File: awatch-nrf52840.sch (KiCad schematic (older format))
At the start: 26 parts, among them U1 nRF52840, X1 ABM11W-32.0000MHZ-8-B1U-T3

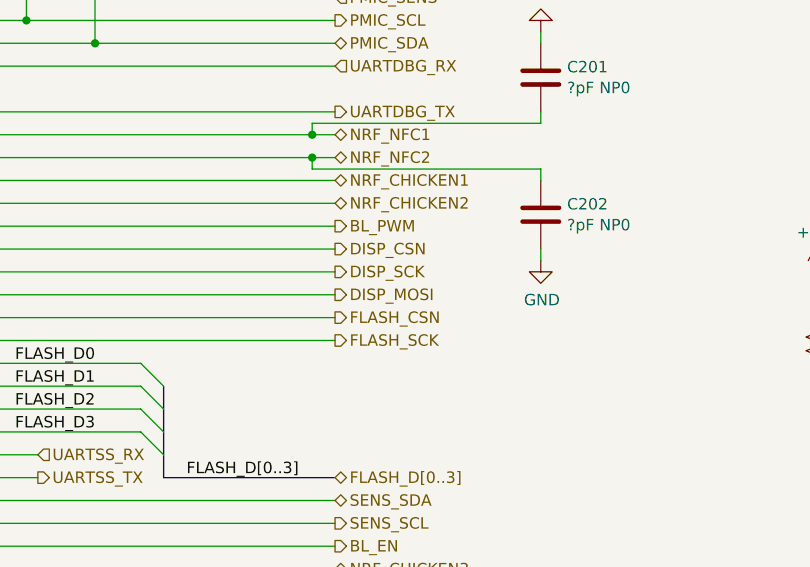
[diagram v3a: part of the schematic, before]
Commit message: fully routed
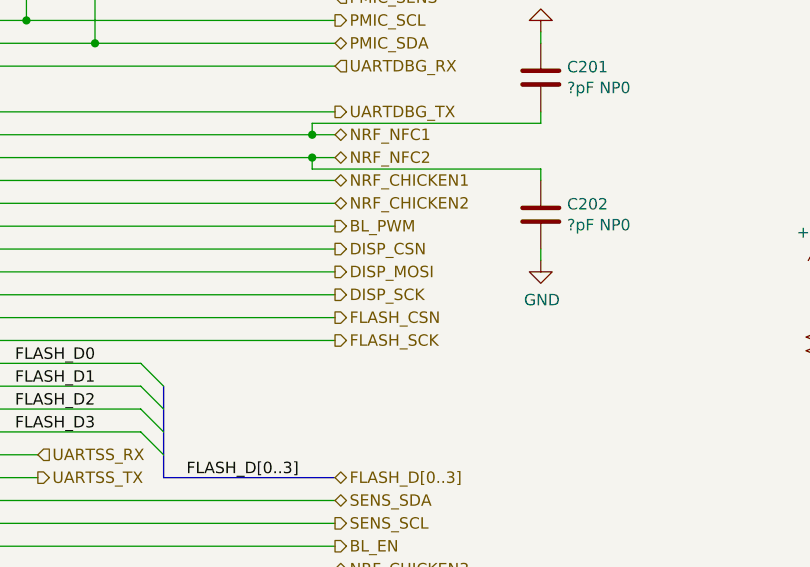
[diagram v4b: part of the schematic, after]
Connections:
- net DISP_MOSI: now also U1.AD10 (P0.15); no longer U1.AC11 (P0.16)
- net DISP_SCK: now also U1.AC11 (P0.16); no longer U1.AD10 (P0.15)
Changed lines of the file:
@@
 Wire Wire Line
 	5150 2500 5650 2500
+Text HLabel 6700 3500 2    50   Output ~ 0
+DISP_MOSI
 Text HLabel 6700 3600 2    50   Output ~ 0
-DISP_MOSI
-Text HLabel 6700 3500 2    50   Output ~ 0
 DISP_SCK
 Text HLabel 6700 3400 2    50   Output ~ 0

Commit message: approx. final layout
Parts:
- C1, C2: DigiKey PN (none) -> 311-3869-1-ND
- C11: DigiKey PN (none) -> 311-1069-1-ND
- C12, C5, C7, C8: value 100nF X7R -> 0.1µF X7R; DigiKey PN (none) -> 1276-1061-1-ND
- C14, C15: DigiKey PN (none) -> 1276-1946-1-ND
- C3, C4: DigiKey PN (none) -> 1276-1293-1-ND
- C6: DigiKey PN (none) -> 1276-2087-1-ND
- C9: DigiKey PN (none) -> 311-3959-1-ND
- U1: DigiKey PN (none) -> 1490-1071-1-ND
- X1: DigiKey PN (none) -> 535-13899-1-ND
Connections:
- net DISP_CSN: now also U1.AC11 (P0.16); no longer U1.AC9 (P0.14)
- net DISP_SCK: now also U1.AC9 (P0.14); no longer U1.AC11 (P0.16)
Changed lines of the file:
@@
 $Descr A4 11693 8268
 encoding utf-8
-Sheet 2 9
+Sheet 2 10
 Title "AWatch2"
 Date ""
@@
 F 2 "Package_DFN_QFN:Nordic_AQFN-73-1EP_7x7mm_P0.5mm" H 3850 1600 50  0001 C CNN
 F 3 "http://infocenter.nordicsemi.com/topic/com.nordic.infocenter.nrf52/dita/nrf52/chips/nrf52840.html" H 3200 6400 50  0001 C CNN
+F 4 "1490-1071-1-ND" H 3850 4500 50  0001 C CNN "DigiKey PN"
 	1    3850 4500
 	1    0    0    -1
@@
 F 2 "Crystal:Crystal_SMD_2016-4Pin_2.0x1.6mm" H 2100 4500 50  0001 C CNN
 F 3 "~" H 2100 4500 50  0001 C CNN
+F 4 "535-13899-1-ND" H 0   0   50  0001 C CNN "DigiKey PN"
 	1    2100 4500
 	0    -1   -1   0
@@
 F 2 "Capacitor_SMD:C_0603_1608Metric" H 2238 4850 50  0001 C CNN
 F 3 "~" H 2200 5000 50  0001 C CNN
+F 4 "311-3869-1-ND" H 0   0   50  0001 C CNN "DigiKey PN"
 	1    2200 5000
 	1    0    0    -1
@@
 F 2 "Capacitor_SMD:C_0603_1608Metric" H 2538 4850 50  0001 C CNN
 F 3 "~" H 2500 5000 50  0001 C CNN
+F 4 "311-3869-1-ND" H 0   0   50  0001 C CNN "DigiKey PN"
 	1    2500 5000
 	1    0    0    -1
@@
 P 2700 1300
 F 0 "C5" H 2609 1346 50  0000 R CNN
-F 1 "100nF X7R" H 2609 1255 50  0000 R CNN
+F 1 "0.1µF X7R" H 2609 1255 50  0000 R CNN
 F 2 "Capacitor_SMD:C_0603_1608Metric" H 2700 1300 50  0001 C CNN
 F 3 "~" H 2700 1300 50  0001 C CNN
+F 4 "1276-1061-1-ND" H 0   0   50  0001 C CNN "DigiKey PN"
 	1    2700 1300
 	1    0    0    -1
@@
 F 2 "Capacitor_SMD:C_0603_1608Metric" H 3000 1300 50  0001 C CNN
 F 3 "~" H 3000 1300 50  0001 C CNN
+F 4 "311-1069-1-ND" H 0   0   50  0001 C CNN "DigiKey PN"
 	1    3000 1300
 	1    0    0    -1
@@
 F 2 "Capacitor_SMD:C_0603_1608Metric" H 3200 1300 50  0001 C CNN
 F 3 "~" H 3200 1300 50  0001 C CNN
+F 4 "1276-1946-1-ND" H 0   0   50  0001 C CNN "DigiKey PN"
 	1    3200 1300
 	1    0    0    -1
@@
 F 2 "Capacitor_SMD:C_0603_1608Metric" H 3500 1300 50  0001 C CNN
 F 3 "~" H 3500 1300 50  0001 C CNN
+F 4 "311-3959-1-ND" H 0   0   50  0001 C CNN "DigiKey PN"
 	1    3500 1300
 	1    0    0    -1
@@
 P 900 1150
 F 0 "C7" H 992 1196 50  0000 L CNN
-F 1 "100nF X7R" H 992 1105 50  0000 L CNN
+F 1 "0.1µF X7R" H 992 1105 50  0000 L CNN
 F 2 "Capacitor_SMD:C_0603_1608Metric" H 900 1150 50  0001 C CNN
 F 3 "~" H 900 1150 50  0001 C CNN
+F 4 "1276-1061-1-ND" H 0   0   50  0001 C CNN "DigiKey PN"
 	1    900  1150
 	1    0    0    -1
@@
 P 1350 1150
 F 0 "C8" H 1442 1196 50  0000 L CNN
-F 1 "100nF X7R" H 1442 1105 50  0000 L CNN
+F 1 "0.1µF X7R" H 1442 1105 50  0000 L CNN
 F 2 "Capacitor_SMD:C_0603_1608Metric" H 1350 1150 50  0001 C CNN
 F 3 "~" H 1350 1150 50  0001 C CNN
+F 4 "1276-1061-1-ND" H 0   0   50  0001 C CNN "DigiKey PN"
 	1    1350 1150
 	1    0    0    -1
@@
 P 1800 1150
 F 0 "C12" H 1892 1196 50  0000 L CNN
-F 1 "100nF X7R" H 1892 1105 50  0000 L CNN
+F 1 "0.1µF X7R" H 1892 1105 50  0000 L CNN
 F 2 "Capacitor_SMD:C_0603_1608Metric" H 1800 1150 50  0001 C CNN
 F 3 "~" H 1800 1150 50  0001 C CNN
+F 4 "1276-1061-1-ND" H 0   0   50  0001 C CNN "DigiKey PN"
 	1    1800 1150
 	1    0    0    -1
@@
 F 2 "Capacitor_SMD:C_0603_1608Metric" H 2400 2900 50  0001 C CNN
 F 3 "~" H 2400 2900 50  0001 C CNN
+F 4 "1276-1293-1-ND" H 0   0   50  0001 C CNN "DigiKey PN"
 	1    2400 2900
 	1    0    0    -1
@@
 Text HLabel 6700 3500 2    50   Output ~ 0
 DISP_MOSI
+Text HLabel 6700 3400 2    50   Output ~ 0
+DISP_SCK
 Text HLabel 6700 3600 2    50   Output ~ 0
-DISP_SCK
-Text HLabel 6700 3400 2    50   Output ~ 0
 DISP_CSN
 Wire Wire Line
@@
 F 2 "Capacitor_SMD:C_0603_1608Metric" H 1350 2250 50  0001 C CNN
 F 3 "~" H 1350 2250 50  0001 C CNN
+F 4 "1276-1946-1-ND" H 0   0   50  0001 C CNN "DigiKey PN"
 	1    1350 2250
 	1    0    0    -1
@@
 F 2 "Capacitor_SMD:C_0603_1608Metric" H 900 2250 50  0001 C CNN
 F 3 "~" H 900 2250 50  0001 C CNN
+F 4 "1276-2087-1-ND" H 0   0   50  0001 C CNN "DigiKey PN"
 	1    900  2250
 	1    0    0    -1
@@
 F 2 "Capacitor_SMD:C_0603_1608Metric" H 1900 2900 50  0001 C CNN
 F 3 "~" H 1900 2900 50  0001 C CNN
+F 4 "1276-1293-1-ND" H 0   0   50  0001 C CNN "DigiKey PN"
 	1    1900 2900
 	1    0    0    -1

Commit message: BOM fully populated
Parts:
- L1: DigiKey PN (none) -> 712-1429-1-ND
- L2: DigiKey PN (none) -> 445-6755-1-ND
- L3: DigiKey PN (none) -> CI160808-15NJCT-ND
- R1, R2, R3, R4: DigiKey PN (none) -> MCT0603-2.20K-CFCT-ND
- R201: DigiKey PN (none) -> MCT0603-10.0K-CFCT-ND
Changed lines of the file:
@@
 F 2 "Inductor_SMD:L_0603_1608Metric" H 4250 1450 50  0001 C CNN
 F 3 "~" H 4250 1450 50  0001 C CNN
+F 4 "445-6755-1-ND" H 0   0   50  0001 C CNN "DigiKey PN"
 	1    4250 1450
 	1    0    0    -1
@@
 F 2 "Inductor_SMD:L_0603_1608Metric" H 4250 1150 50  0001 C CNN
 F 3 "~" H 4250 1150 50  0001 C CNN
+F 4 "CI160808-15NJCT-ND" H 0   0   50  0001 C CNN "DigiKey PN"
 	1    4250 1150
 	1    0    0    -1
@@
 F 2 "Inductor_SMD:L_0603_1608Metric" H 2150 2700 50  0001 C CNN
 F 3 "~" H 2150 2700 50  0001 C CNN
+F 4 "712-1429-1-ND" H 0   0   50  0001 C CNN "DigiKey PN"
 	1    2150 2700
 	0    -1   -1   0
@@
 F 2 "Resistor_SMD:R_0603_1608Metric" H 5350 1700 50  0001 C CNN
 F 3 "~" H 5350 1700 50  0001 C CNN
+F 4 "MCT0603-2.20K-CFCT-ND" H 0   0   50  0001 C CNN "DigiKey PN"
 	1    5350 1700
 	1    0    0    -1
@@
 F 2 "Resistor_SMD:R_0603_1608Metric" H 5650 1700 50  0001 C CNN
 F 3 "~" H 5650 1700 50  0001 C CNN
+F 4 "MCT0603-2.20K-CFCT-ND" H 0   0   50  0001 C CNN "DigiKey PN"
 	1    5650 1700
 	1    0    0    -1
@@
 F 2 "Resistor_SMD:R_0603_1608Metric" H 8800 3800 50  0001 C CNN
 F 3 "~" H 8800 3800 50  0001 C CNN
+F 4 "MCT0603-2.20K-CFCT-ND" H 0   0   50  0001 C CNN "DigiKey PN"
 	1    8800 3800
 	1    0    0    -1
@@
 F 2 "Resistor_SMD:R_0603_1608Metric" H 9100 3800 50  0001 C CNN
 F 3 "~" H 9100 3800 50  0001 C CNN
+F 4 "MCT0603-2.20K-CFCT-ND" H 0   0   50  0001 C CNN "DigiKey PN"
 	1    9100 3800
 	1    0    0    -1
@@
 F 2 "Resistor_SMD:R_0603_1608Metric" H 5800 5100 50  0001 C CNN
 F 3 "~" H 5800 5100 50  0001 C CNN
+F 4 "MCT0603-10.0K-CFCT-ND" H 0   0   50  0001 C CNN "DigiKey PN"
 	1    5800 5100
 	1    0    0    -1
